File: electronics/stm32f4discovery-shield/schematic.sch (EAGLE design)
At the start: 1 part

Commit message: Iniciando o routing.
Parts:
- added C1: 104, SparkFun-Capacitors:0.1UF-50V-20%(PTH)KIT-EZ
- added C2, C3: (no value), SparkFun-Capacitors:0.1UF-50V-20%(PTH)KIT-EZ
- added ESC, JP1: (no value), con-lstb:MA03-2
- added I2C1_ESC, I2C3_IMU, SPI1, US2, US5_SONAR, US6: RJ11-2L-B, con-tycoelectronics:RJ11-2L-B
- added IC1: MAX3468CPA, maxim:MAX3468CPA
- added IC2: (no value), SparkFun-PowerIC:V_REG_78XX-TO-220
- added IC3, IC4: LM340H-12, linear:LM340H-12
- added ISP1: AVRISP-6, adafruit:AVRISP-6
- added J1: POWER_JACKSLT, SparkFun-Connectors:POWER_JACKSLT
- added JP2, JP3: (no value), SparkFun-Passives:JUMPER-2PTH
- added JP4: (no value), jumper:JP2E
- added LED1, LED2, LED_PWR: (no value), adafruit:LED5MM
- added Q1: BC548, transistor-npn:BC548
- added R1, R3: (no value), adafruit:R-US_M1206
- added R10, R4, R5, R6, R7, R8, R9: (no value), adafruit:R-US_0204/7
- added R2: (no value), rcl:R-EU_0204/2V
- added RECV, SV1, SV2, SV3: (no value), con-lstb:MA03-1
- added SJ1: (no value), jumper:SJ2WW
- added SRVO1, SRVO2: (no value), SparkFun-Connectors:M04POLAR
- added U$2: JYMCU_LOGIC_LEVEL_CONVERTER, provant_custom:JYMCU_LOGIC_LEVEL_CONVERTER
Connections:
- new net 3.3V: I2C1_ESC.1, I2C3_IMU.1, R1.2, R3.2, U$1.VDD2, U$1.VDD3, U$2.3V3, US2.1, US5_SONAR.1, US6.1
- new net 5V: C1.1, I2C1_ESC.2, I2C3_IMU.2, IC1.VCC, ISP1.VCC, JP4.2, R10.1, R2.2, R4.2, R9.1, RECV.2, SPI1.2, SV1.2, SV2.2, SV3.2, U$1.5V, U$1.5V2, U$2.5V, US2.2, US5_SONAR.2, US6.2
- new net 5V_REG: C3.1, IC2.OUT, JP4.1
- new net D+/TX: IC1.A, JP3.2, SRVO1.3, SRVO2.3
- new net D-/RX: IC1.B, JP2.2, SRVO1.4, SRVO2.4
- new net GND: C1.2, C2.2, C3.2, ESC.1, ESC.2, I2C1_ESC.5, I2C1_ESC.6, I2C3_IMU.5, I2C3_IMU.6, IC1.GND, IC2.GND, ISP1.GND, J1.GND, J1.GNDBREAK, LED_PWR.C, Q1.E, R6.2, R8.2, RECV.3, SPI1.6, SRVO1.1, SRVO2.1, SV1.3, SV2.3, SV3.3, U$1.GND, U$1.GND1, U$1.GND2, U$1.GND3, U$1.GND4, U$1.GND5, U$1.GND6, U$1.GND7, U$1.GND8, U$1.GND9, U$2.GND1, U$2.GND2, US2.5, US2.6, US5_SONAR.5, US5_SONAR.6, US6.5, US6.6
- new net N$1: JP1.5, U$2.D_L
- new net N$2: JP1.6, U$2.C_L
- new net N$3: Q1.C, R2.1, SJ1.3
- new net N$4: LED_PWR.A, R4.1
- new net N$5: LED1.A, R9.2
- new net N$6: IC3.GND, R5.1, R6.1
- new net N$7: LED2.A, R10.2
- new net N$8: IC4.GND, R7.2, R8.1
- new net PA2/USART2_TX: U$1.PA2, US2.3
- new net PA3/USART2_RX: U$1.PA3, US2.4
- new net PA8/I2C3_SCL: JP1.4, U$1.PA8
- new net PB0/PWM: LED2.C
- new net PB1/PWM: LED1.C
- new net PB3/SPI1_SCK: ISP1.SCK, SPI1.5, U$1.PB3
- new net PB4/SPI1_MISO: ISP1.MISO, SPI1.4, U$1.PB4
- new net PB5/SPI1_MOSI: ISP1.MOSI, SPI1.3, U$1.PB5
- new net PB6/USART1_TX: IC1.DI, JP3.1, U$1.PB6
- new net PB7/USART1_RX: IC1.RO, JP2.1, U$1.PB7
- new net PB8/I2C1_SCL: U$1.PB8, U$2.B_L
- new net PB9/I2C1_SDA: U$1.PB9, U$2.A_L
- new net PC10/USART3_TX: U$1.PC10, US5_SONAR.3
- new net PC11/USART3_RX: SJ1.2, U$1.PC11
- new net PC6/USART6_TX: U$1.PC6, US6.3
- new net PC7/USART6_RX: U$1.PC7, US6.4
- new net PC9/I2C3_SDA: JP1.3, U$1.PC9
- new net PE11/PWM: SV3.1
- new net PE13/PWM: SV2.1
- new net PE14/PWM: SV1.1
- new net PE2: IC1.DE, IC1.RE/, U$1.PE2
- new net PE9/PWM: RECV.1
- new net SCL1: ESC.5, ESC.6, I2C1_ESC.4, U$2.B_H
- new net SCL2: I2C3_IMU.4, JP1.2, R3.1, U$2.C_H
- new net SDA1: ESC.3, ESC.4, I2C1_ESC.3, U$2.A_H
- new net SDA2: I2C3_IMU.3, JP1.1, R1.1, U$2.D_H
- new net SONAR_RX: Q1.B, SJ1.1, US5_SONAR.4
- new net SRVO1_PWR: IC4.VO, R7.1, SRVO1.2
- new net SRVO2_PWR: IC3.VO, R5.2, SRVO2.2
- new net VCC: C2.1, IC2.IN, IC3.VI, IC4.VI, J1.PWR, JP4.3
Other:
- note added: "* Conversor eh necessario?"
- note added: "* JP4 pode bypassar o regulador se forem fornecidos 5V regulados. * IC2 nao vem montado por default. * IC3 e IC4 nao vem montados por default."
- note added: "* JPI permite escolher se vai se fazer uso do conversor com pull-ups."
- note added: "* Para os servos RX24f, montar IC1. * Para servos Dongbu, remover IC1, e bypassar linhas de TX e RX atraves de JP1 e JP2."
- note added: "* Para sonar XL-MaxSonar-EZ MB1200, soldar SJ1 na posiçao 2-3. * Para usar como linha de serial comum, soldar SJ1 na posiçao 1-2."
- note added: "* R1 e R3 nao estao montados por default."
- note added: "IMU & ESC"
- note added: "POWER"
- note added: "SERVO"
- note added: "SONAR"
- note added: "SONAR & Perifericos"

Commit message: Primeira versao para fabricacao da placa STM32 Discovery.
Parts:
- removed ISP1: AVRISP-6, adafruit:AVRISP-6
- removed JP2, JP3: (no value), SparkFun-Passives:JUMPER-2PTH
- removed JP4: (no value), jumper:JP2E
- added SJ3: (no value), SparkFun-Passives:SOLDERJUMPER_2WAY-OLDW
- R2: device rcl:R-EU_0204/2V -> rcl:R-EU_0204/5
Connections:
- removed net 5V_REG: C3.1, IC2.OUT, JP4.1
- net 3.3V: no longer I2C1_ESC.1, US5_SONAR.1, US6.1
- net 5V: now also C3.1, IC2.OUT, SJ3.3; no longer ISP1.VCC, JP4.2
- net D+/TX: no longer JP3.2
- net D-/RX: no longer JP2.2
- net GND: no longer ISP1.GND
- net PB0/PWM: now also LED1.C, U$1.PB0; no longer LED2.C
- net PB1/PWM: now also LED2.C, U$1.PB1; no longer LED1.C
- net PB3/SPI1_SCK: now also SPI1.3; no longer ISP1.SCK, SPI1.5
- net PB4/SPI1_MISO: no longer ISP1.MISO
- net PB5/SPI1_MOSI: now also SPI1.5; no longer ISP1.MOSI, SPI1.3
- net PB6/USART1_TX: no longer JP3.1
- net PB7/USART1_RX: no longer JP2.1
- net PE11/PWM: now also SV1.1, U$1.PE11; no longer SV3.1
- net PE13/PWM: now also U$1.PE13
- net PE14/PWM: now also SV3.1, U$1.PE14; no longer SV1.1
- net PE9/PWM: now also U$1.PE9
- net VCC: now also SJ3.1, SJ3.2; no longer JP4.3
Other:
- note added: "* SJ3 pode ser soldado caso IC2 nao esteja montado e 5V regulados sejam fornecidos. * IC2 nao vem montado por default. * IC3 e IC4 nao vem montados por default."
- note removed: "* JP4 pode bypassar o regulador se forem fornecidos 5V regulados. * IC2 nao vem montado por default. * IC3 e IC4 nao vem montados por default."

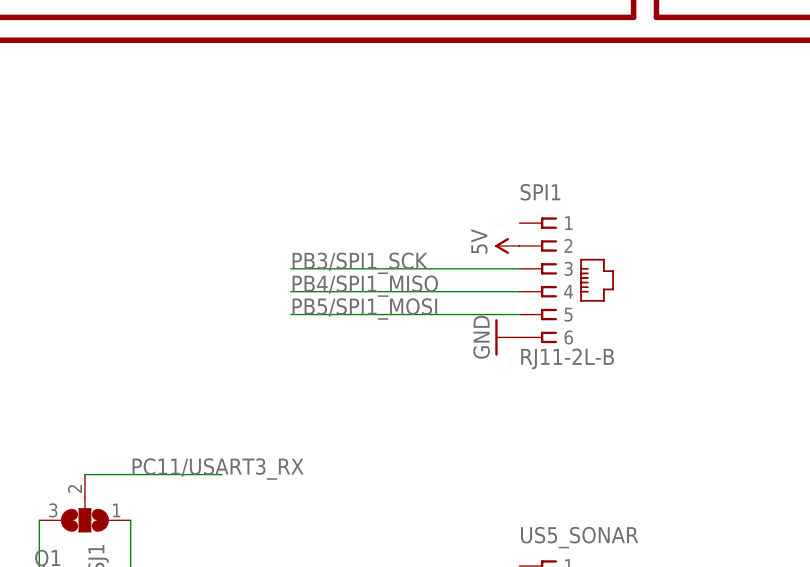
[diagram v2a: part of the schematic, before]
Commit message: Alterados os pads do componente da STM32F4-Discovery (pads octogonais, 0.066 com o menor drill). Conectores alterados para serem compatíveis com plugs RJ11 (usando principalmente as 4 vias do centro).
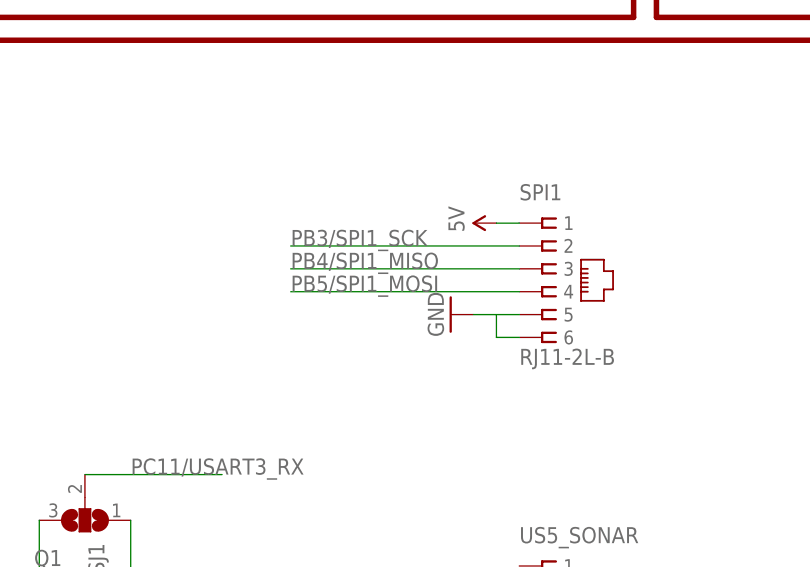
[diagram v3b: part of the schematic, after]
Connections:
- net 5V: now also SPI1.1; no longer SPI1.2
- net GND: now also SPI1.5
- net PB3/SPI1_SCK: now also SPI1.2; no longer SPI1.3
- net PB4/SPI1_MISO: now also SPI1.3; no longer SPI1.4
- net PB5/SPI1_MOSI: now also SPI1.4; no longer SPI1.5
